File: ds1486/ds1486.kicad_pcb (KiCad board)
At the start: 4 copper layers, 30.4 x 43.9 mm, 71 parts, among them J1 DBG, J2 DBG1-16, J3 DBG17-32, J4 DS1-16, J5 DS17-32, U1 RP2040, U3 AMS1117-3.3, U4 SN74LVC8T245, U5 SN74LVC1G00DRL, U6 YSN8010SJ, U7 SN74LVC1G00DRL, U8 W25Q16JVSS, Y2 E3SB12E00004EE

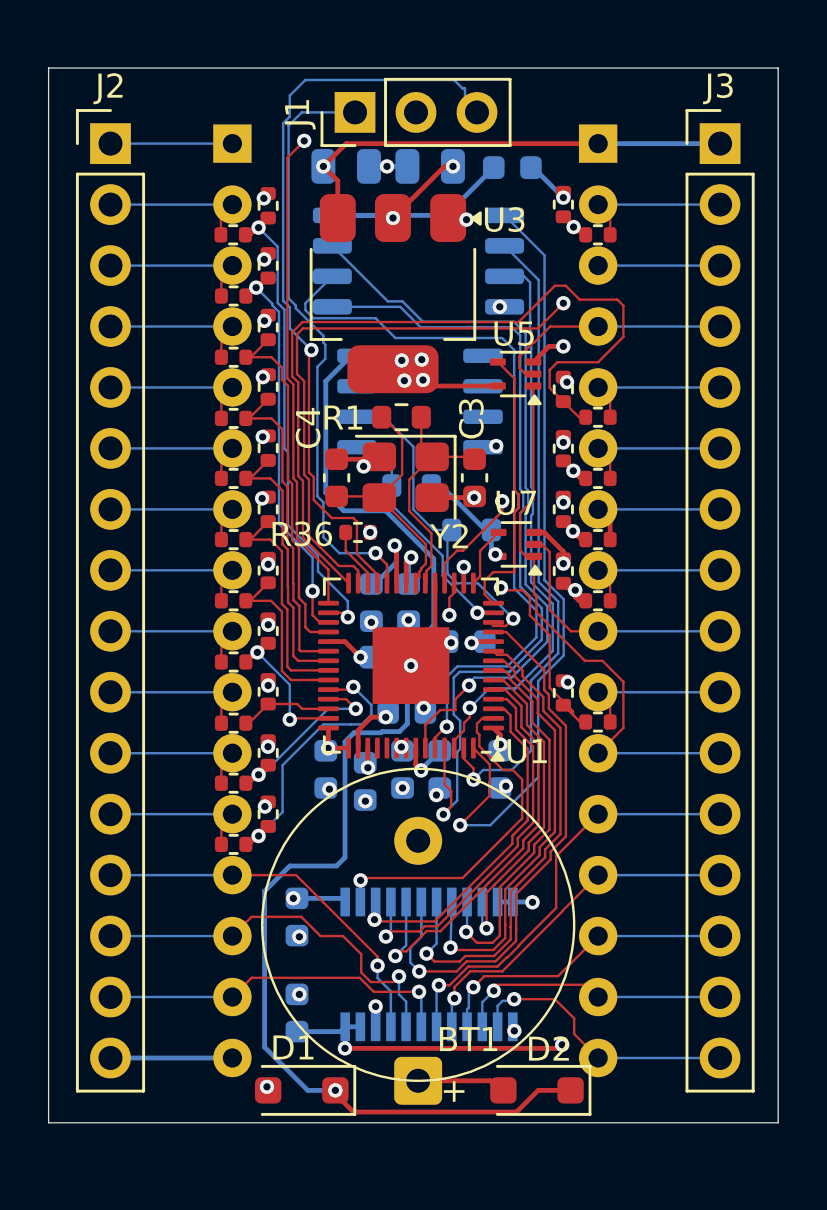
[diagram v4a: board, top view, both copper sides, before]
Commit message: Add some decoupling caps. Gerbers.
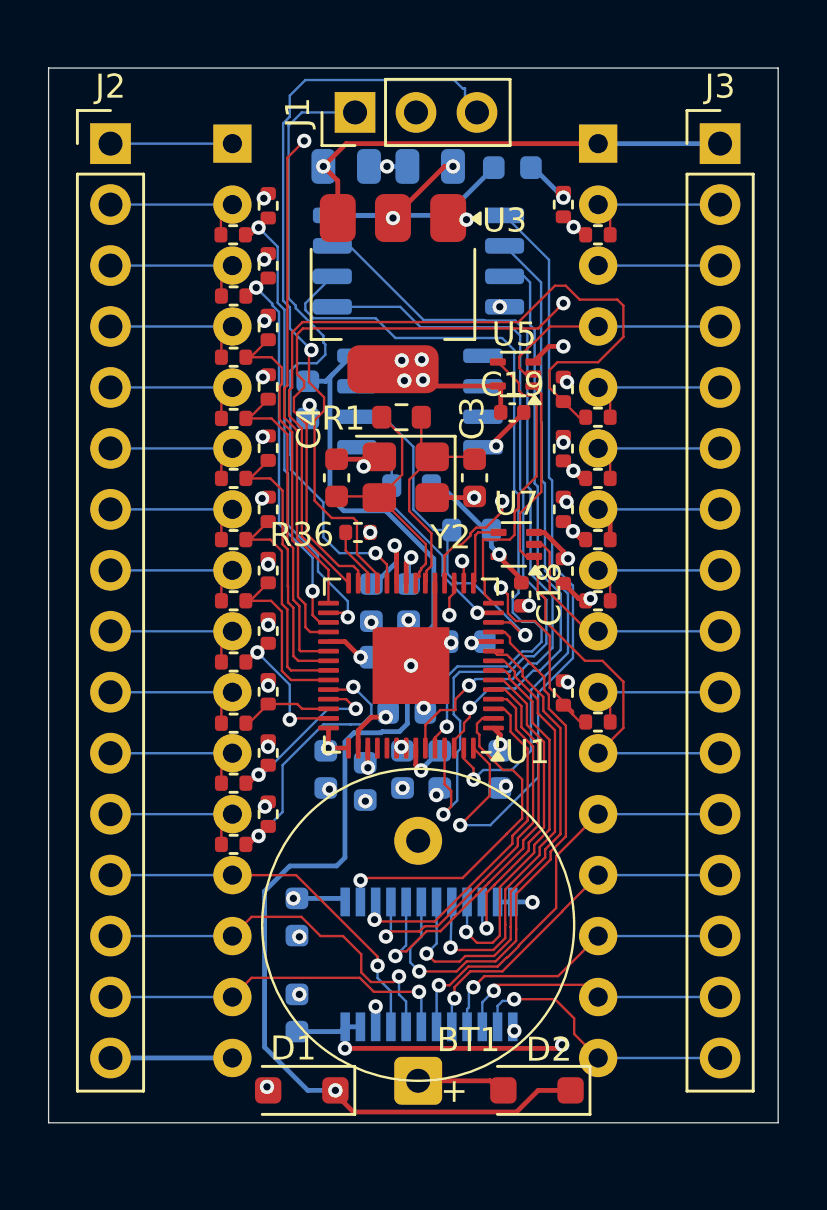
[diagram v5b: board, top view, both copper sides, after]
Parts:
- added C18: 100n, Capacitor_SMD:C_0402_1005Metric, F.Cu at (123.8, 82.3)
- added C19: 100n, Capacitor_SMD:C_0402_1005Metric, F.Cu at (123.4, 74.7)
- added C20: 100n, Capacitor_SMD:C_0603_1608Metric, B.Cu at (114.9, 74.2)
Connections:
- U6 pad 3: Net-(U6-FOUT) -> unconnected-(U6-FOUT-Pad3)
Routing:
- net +3V3: track 67.3 -> 70.3 mm
- net GND: track 31.8 -> 34.6 mm, vias 39 -> 41
- net /SWCLK: track 24.9 -> 26.3 mm
- net /SCL: track 13.8 -> 15.2 mm
- net /AC11: track 8.97 -> 10.0 mm
- net /CE_WE: track 11.7 -> 12.7 mm
- net /VRTC: track 51.7 -> 52.7 mm
- net /QSPI_SCLK: track 31.4 -> 32.2 mm
- net /QSPI_SD3: track 30.7 -> 31.3 mm
- net /AC10: track 11.1 -> 11.6 mm

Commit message: Move VRTC and SPI flash to front layer.
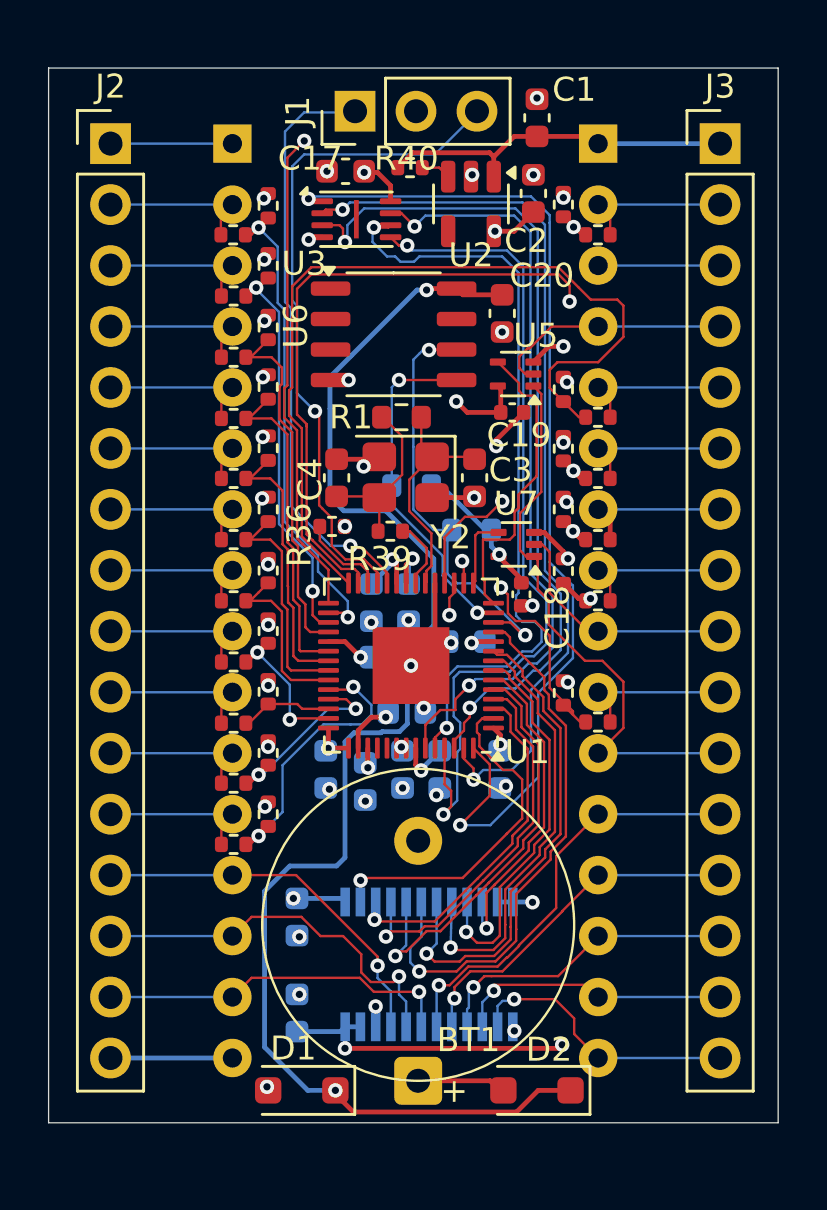
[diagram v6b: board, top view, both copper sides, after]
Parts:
- removed U8: W25Q16JVSS, Package_SO:SOIC-8_5.3x5.3mm_P1.27mm
- added R39: 1k, Resistor_SMD:R_0402_1005Metric, F.Cu at (118.3, 79.7)
- added R40: 10k, Resistor_SMD:R_0402_1005Metric, F.Cu at (119.2, 64.5)
- added U2: AP2112K-3.3, Package_TO_SOT_SMD:SOT-23-5, F.Cu at (121.7, 66.0)
- C1, C2: value C_Polarized -> 1u; footprint Capacitor_SMD:C_0805_2012Metric -> Capacitor_SMD:C_0603_1608Metric; moved to F.Cu
- C17, C20, U6: moved to F.Cu
- C3, C4: value C -> 15p
- R20, R21, R22, R23, R24, R25, R26, R27, R28, R29, R3, R30, R31, R32, R33, R34, R35: value 3k -> 1.96k
- U3: value AMS1117-3.3 -> W25Q16JVUXIQ; footprint Package_TO_SOT_SMD:SOT-223-3_TabPin2 -> Package_SON:Winbond_USON-8-1EP_3x2mm_P0.5mm_EP0.2x1.6mm
- moved C20 8.86 mm to (123.0, 70.6)
- moved C1 8.20 mm to (124.5, 62.4), turned to 90 degrees
- moved C17 6.95 mm to (116.5, 64.7), turned to 180 degrees
- moved C2 4.44 mm to (124.3, 65.6), turned to 90 degrees
- moved U3 3.45 mm to (116.9, 66.7), turned to 0 degrees
- moved U6 3.01 mm to (118.5, 71.4), turned to 0 degrees
- moved R36 1.11 mm to (115.9, 79.5)
- moved J1 0.05 mm to (116.9, 62.1)
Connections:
- C4 pad 1: /XOUT -> Net-(C4-Pad1)
- R1 pad 2: /XOUT -> Net-(C4-Pad1)
- U3 pad 1: GND -> /QSPI_SS
- U3 pad 2: +3V3 -> /QSPI_SD1
- U3 pad 3: +5V -> /QSPI_SD2
- Y2 pad 3: /XOUT -> Net-(C4-Pad1)
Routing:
- net +3V3: track 70.3 -> 55.4 mm, vias 17 -> 14
- net /QSPI_SD2: track 23.7 -> 35.5 mm, vias 1 -> 2
- net /QSPI_SS: track 33.3 -> 43.5 mm, vias 1 -> 2
- net /QSPI_SD1: track 27.1 -> 37.2 mm, vias 1 -> 2
- net /XOUT: track 10.6 -> 2.94 mm
- net Net-(C4-Pad1): track 0.00 -> 7.37 mm
- net /VRTC: track 52.7 -> 59.1 mm, vias 1 -> 2
- net +5V: track 72.8 -> 68.5 mm, vias 3 -> 2
- net /SDA: track 10.7 -> 14.7 mm, vias 1 -> 2
- net GND: track 34.6 -> 30.8 mm, vias 41 -> 44
- net /SWD: track 31.9 -> 28.4 mm
- net /SCL: track 15.2 -> 17.9 mm, vias 1 -> 2
- net /AC8: track 36.1 -> 38.2 mm
- net +1V1: track 18.9 -> 17.1 mm
- net /AC13: track 34.2 -> 35.9 mm
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
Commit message: Move D_DIR.
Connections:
- U1 pad 11: /DQC7 -> /D_DIR
- U1 pad 2: /D_DIR -> /DQC0
- U1 pad 3: /DQC0 -> /DQC1
- U1 pad 4: /DQC1 -> /DQC2
- U1 pad 5: /DQC2 -> /DQC3
- U1 pad 6: /DQC3 -> /DQC4
- U1 pad 7: /DQC4 -> /DQC5
- U1 pad 8: /DQC5 -> /DQC6
- U1 pad 9: /DQC6 -> /DQC7
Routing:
- net /D_DIR: track 14.5 -> 19.2 mm
- net /DQC3: track 14.5 -> 12.6 mm
- net /DQC7: track 23.1 -> 21.6 mm
- net /DQC6: track 20.6 -> 19.5 mm
- net /DQC5: track 18.5 -> 17.5 mm
- net /DQC1: track 16.0 -> 14.9 mm
- net /DQC2: track 17.6 -> 16.5 mm
- net /DQC0: track 14.6 -> 13.6 mm
- net GND: track 30.8 -> 31.5 mm
- net /DQC4: track 15.7 -> 15.1 mm
- net /QSPI_SD1: track 37.2 -> 36.7 mm

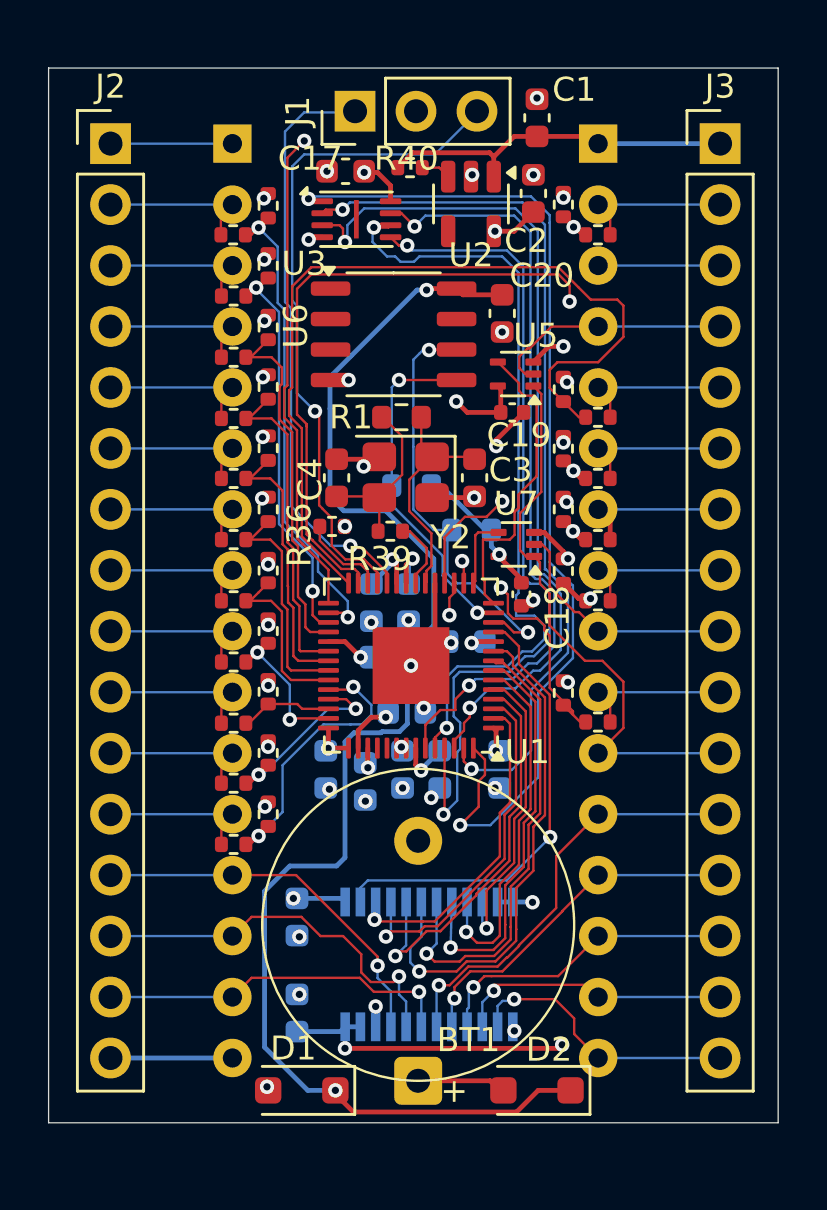
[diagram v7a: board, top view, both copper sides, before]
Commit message: Remove old W25Q16.
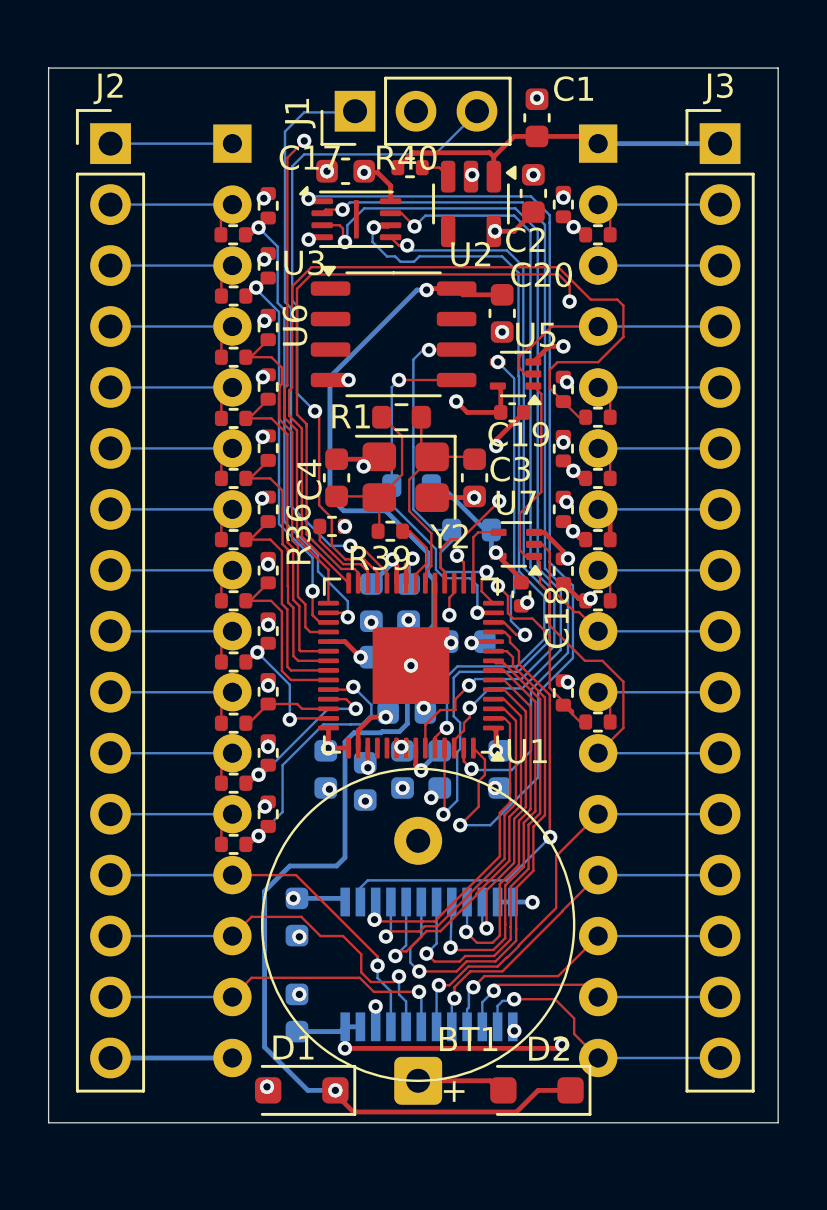
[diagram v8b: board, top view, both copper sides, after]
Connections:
- U1 pad 12: /SCL -> /CE_WE
- U1 pad 14: /CE_WE -> /SCL
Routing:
- net /SCL: track 18.1 -> 15.5 mm
- net /CE_WE: track 12.7 -> 13.5 mm, vias 0 -> 2
- net /SDA: track 14.7 -> 15.4 mm
- net /QSPI_SCLK: track 32.4 -> 31.8 mm
